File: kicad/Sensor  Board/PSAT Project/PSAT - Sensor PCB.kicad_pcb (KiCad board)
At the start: 2 copper layers, 120 x 120 mm, 16 parts, among them J1 MCU Conn_01x04, J2 Conn_01x02, J3 Conn_01x03, J4 Conn_01x03, J5 Conn_01x01, U1 MPU-6000, U2 BME280

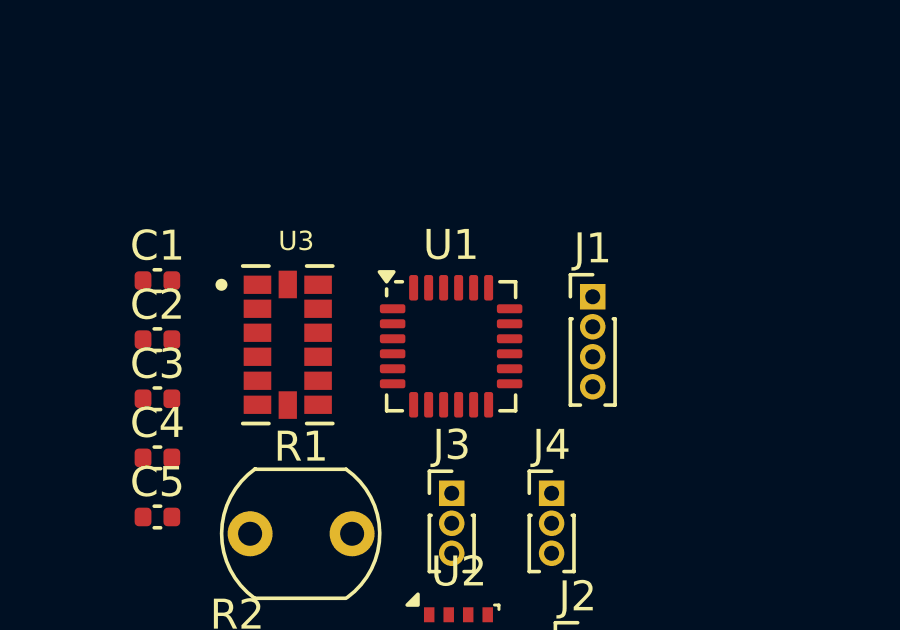
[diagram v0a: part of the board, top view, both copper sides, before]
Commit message: Updated Sensor board: Pin corrections + added footprint
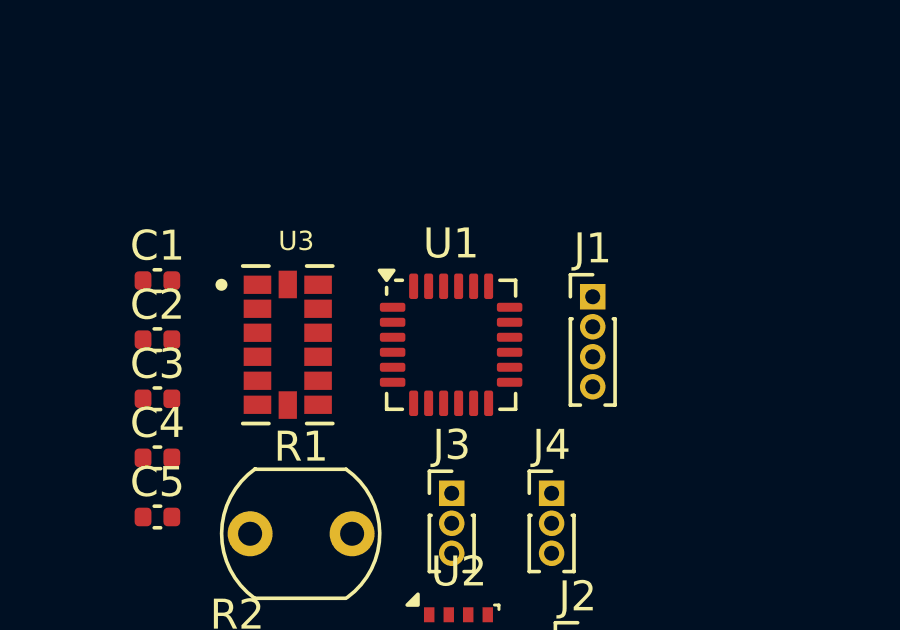
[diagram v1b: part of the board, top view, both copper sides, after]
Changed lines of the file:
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@@
 	(footprint "Sensor_Motion:InvenSense_QFN-24_4x4mm_P0.5mm"
 		(layer "F.Cu")
-		(at 105.78 90.05)
+		(at 105.78 90)
 		(descr "24-Lead Plastic QFN (4mm x 4mm); Pitch 0.5mm; EP 2.7x2.6mm; for InvenSense motion sensors; keepout area marked (Package see: https://store.invensense.com/datasheets/invensense/MPU-6050_DataSheet_V3%204.pdf; See also https://www.invensense.com/wp-content/uploads/2015/02/InvenSense-MEMS-Handling.pdf)")
 		(tags "QFN 0.5")
@@
 			(polygon
 				(pts
-					(xy 104.405 88.725) (xy 107.155 88.725) (xy 107.155 91.375) (xy 104.405 91.375)
-				)
-			)
+					(xy 104.405 88.675) (xy 107.155 88.675) (xy 107.155 91.325) (xy 104.405 91.325)
+				)
+			)
